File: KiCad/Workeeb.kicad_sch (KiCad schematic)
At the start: 227 parts, among them J1 USB_C_Receptacle_USB2.0, U1 EFM32HG322F64G-C-QFP48

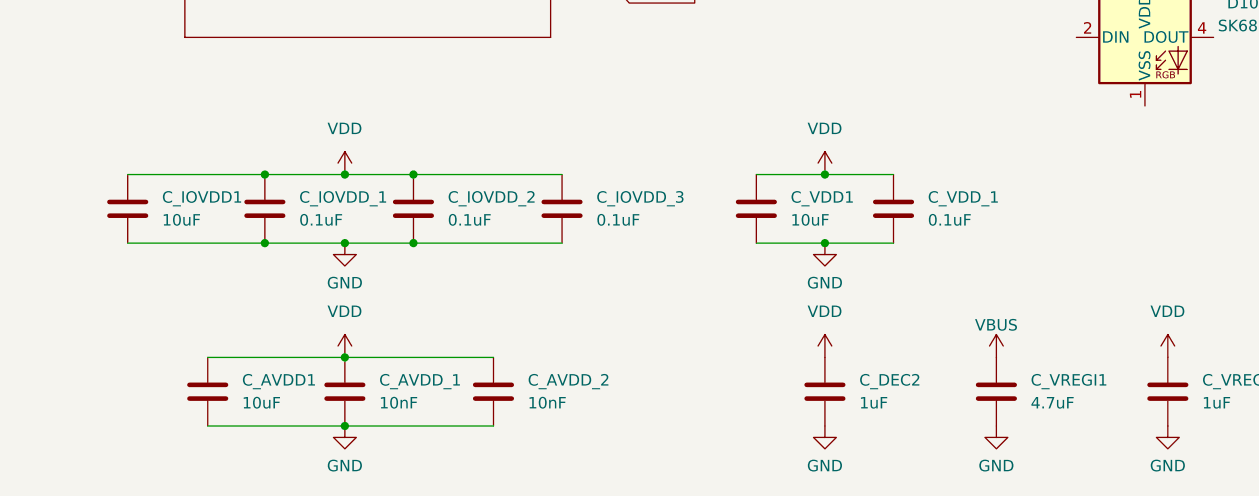
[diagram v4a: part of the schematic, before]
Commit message: Better cap names, start placing decoupling caps
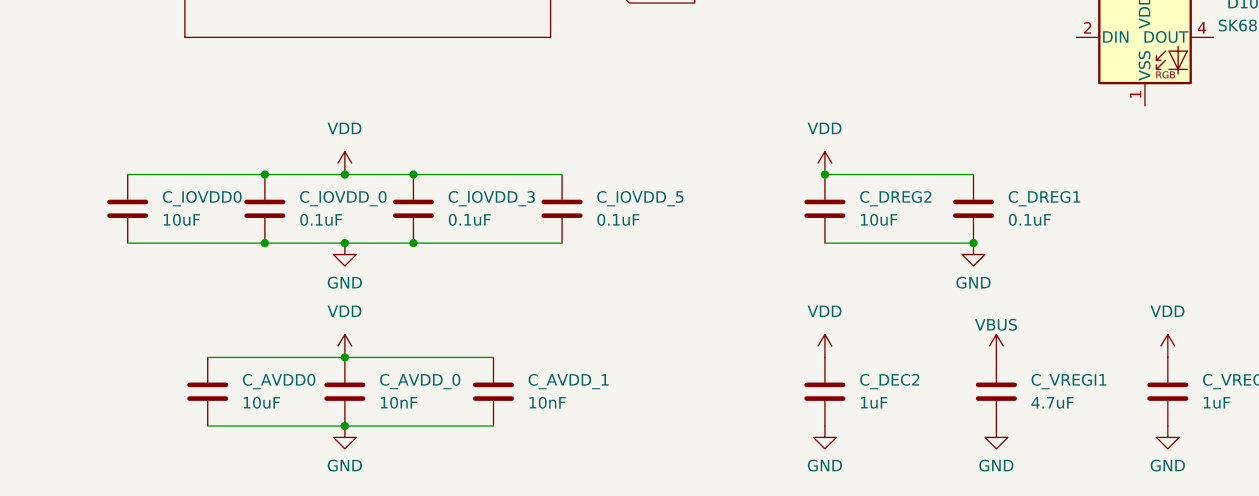
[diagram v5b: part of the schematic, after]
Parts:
- removed C_VDD1: 10uF, Capacitor_SMD:C_0805_2012Metric, symbol Device:C
- removed C_VDD_1: 0.1uF, Capacitor_SMD:C_0805_2012Metric, symbol Device:C
- added C_DREG1: 0.1uF, Capacitor_SMD:C_0402_1005Metric, symbol Device:C
- added C_DREG2: 10uF, Capacitor_SMD:C_0402_1005Metric, symbol Device:C
- C_AVDD0: renamed from C_AVDD1; footprint Capacitor_SMD:C_0805_2012Metric -> Capacitor_SMD:C_0402_1005Metric
- C_AVDD_0: renamed from C_AVDD_1; footprint Capacitor_SMD:C_0805_2012Metric -> Capacitor_SMD:C_0402_1005Metric
- C_AVDD_1: renamed from C_AVDD_2; footprint Capacitor_SMD:C_0805_2012Metric -> Capacitor_SMD:C_0402_1005Metric
- C_DEC1, C_DEC2, C_RESET1, C_VREGI1, C_VREGO1: footprint Capacitor_SMD:C_0805_2012Metric -> Capacitor_SMD:C_0402_1005Metric
- C_IOVDD0: renamed from C_IOVDD1; footprint Capacitor_SMD:C_0805_2012Metric -> Capacitor_SMD:C_0402_1005Metric
- C_IOVDD_0: renamed from C_IOVDD_1; footprint Capacitor_SMD:C_0805_2012Metric -> Capacitor_SMD:C_0402_1005Metric
- C_IOVDD_3: renamed from C_IOVDD_2; footprint Capacitor_SMD:C_0805_2012Metric -> Capacitor_SMD:C_0402_1005Metric
- C_IOVDD_5: renamed from C_IOVDD_3; footprint Capacitor_SMD:C_0805_2012Metric -> Capacitor_SMD:C_0402_1005Metric
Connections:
- net GND: now also C_DREG1.2, C_DREG2.2
- net VDD: now also C_DREG1.1, C_DREG2.1

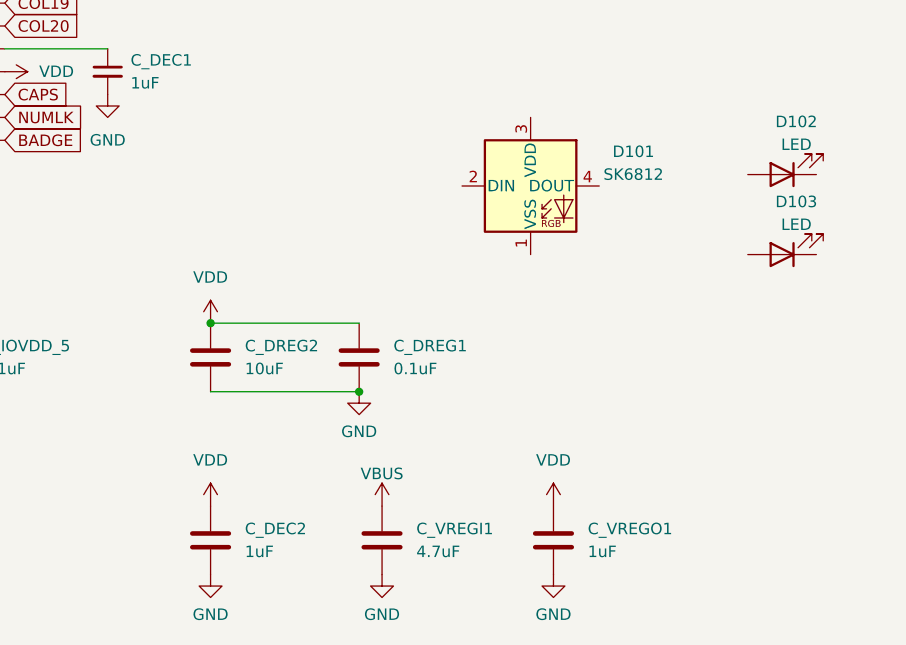
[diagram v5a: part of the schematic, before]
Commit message: Work towards getting decoupling caps and col routes in place
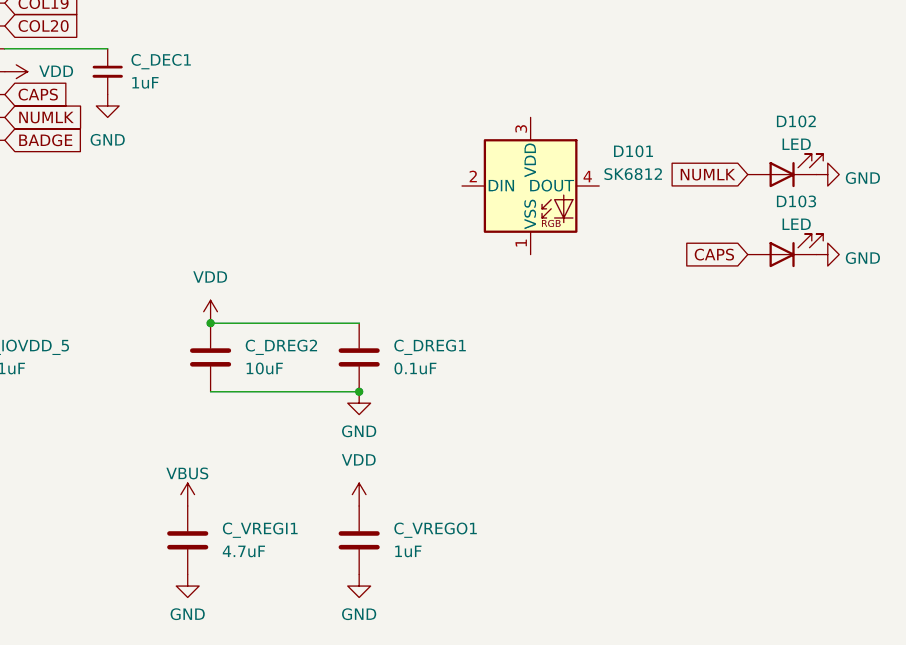
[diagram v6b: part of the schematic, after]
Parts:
- removed C_DEC2: 1uF, Capacitor_SMD:C_0402_1005Metric, symbol Device:C
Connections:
- net CAPS: now also D103.2 (A)
- net GND: now also D102.1 (K), D103.1 (K)
- net NUMLK: now also D102.2 (A)
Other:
- moved on the sheet: C_VREGI1, C_VREGO1

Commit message: Draft finish PCB
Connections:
- net BADGE: now also D101.2 (DIN)
- net GND: now also D101.1 (VSS)
- net VDD: now also D101.3 (VDD)
- no-connect marks 5 -> 6
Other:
- moved on the sheet: D101
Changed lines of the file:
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@@
   (no_connect (at 308.61 100.33))
   (no_connect (at 308.61 107.95))
+  (no_connect (at 421.64 113.03))
   (no_connect (at 330.2 11.43))
   (no_connect (at 330.2 8.89))
@@
     )
   )
+  (global_label "BADGE" (shape input) (at 406.4 113.03 180) (fields_autoplaced)
+    (effects (font (size 1.27 1.27)) (justify right))
+    (property "Intersheet References" "${INTERSHEET_REFS}" (id 0) (at 398.0282 113.1094 0)
+      (effects (font (size 1.27 1.27)) (justify right) hide)
+    )
+  )
   (global_label "COL6" (shape input) (at 81.28 24.13 90) (fields_autoplaced)
     (effects (font (size 1.27 1.27)) (justify left))
@@
     (pin "2")
   )
+  (symbol (lib_id "power:VDD") (at 414.02 105.41 0) (unit 1)
+    (in_bom yes) (on_board yes) (fields_autoplaced)
+    (property "Reference" "#PWR?" (id 0) (at 414.02 109.22 0)
+      (effects (font (size 1.27 1.27)) hide)
+    )
+    (property "Value" "VDD" (id 1) (at 414.02 100.33 0))
+    (property "Footprint" "" (id 2) (at 414.02 105.41 0)
+      (effects (font (size 1.27 1.27)) hide)
+    )
+    (property "Datasheet" "" (id 3) (at 414.02 105.41 0)
+      (effects (font (size 1.27 1.27)) hide)
+    )
+    (pin "1")
+  )
   (symbol (lib_id "power:GND") (at 314.96 19.05 0) (unit 1)
     (in_bom yes) (on_board yes) (fields_autoplaced)
@@
     (pin "2")
   )
+  (symbol (lib_id "power:GND") (at 414.02 120.65 0) (unit 1)
+    (in_bom yes) (on_board yes) (fields_autoplaced)
+    (property "Reference" "#PWR?" (id 0) (at 414.02 127 0)
+      (effects (font (size 1.27 1.27)) hide)
+    )
+    (property "Value" "GND" (id 1) (at 414.02 125.73 0))
+    (property "Footprint" "" (id 2) (at 414.02 120.65 0)
+      (effects (font (size 1.27 1.27)) hide)
+    )
+    (property "Datasheet" "" (id 3) (at 414.02 120.65 0)
+      (effects (font (size 1.27 1.27)) hide)
+    )
+    (pin "1")
+  )
   (symbol (lib_id "Device:D_Small") (at 191.77 106.68 90) (unit 1)
     (in_bom yes) (on_board yes) (fields_autoplaced)
@@
     (pin "1")
   )
-  (symbol (lib_id "LED:SK6812") (at 422.91 113.03 0) (unit 1)
+  (symbol (lib_id "LED:SK6812") (at 414.02 113.03 0) (unit 1)
     (in_bom yes) (on_board yes)
-    (property "Reference" "D101" (id 0) (at 434.34 109.22 0))
-    (property "Value" "SK6812" (id 1) (at 434.34 111.7569 0))
-    (property "Footprint" "LED_SMD:LED_SK6812_PLCC4_5.0x5.0mm_P3.2mm" (id 2) (at 424.18 120.65 0)
+    (property "Reference" "D101" (id 0) (at 425.45 109.22 0))
+    (property "Value" "SK6812" (id 1) (at 425.45 111.7569 0))
+    (property "Footprint" "LED_SMD:LED_SK6812_PLCC4_5.0x5.0mm_P3.2mm" (id 2) (at 415.29 120.65 0)
       (effects (font (size 1.27 1.27)) (justify left top) hide)
     )
-    (property "Datasheet" "https://cdn-shop.adafruit.com/product-files/1138/SK6812+LED+datasheet+.pdf" (id 3) (at 425.45 122.555 0)
+    (property "Datasheet" "https://cdn-shop.adafruit.com/product-files/1138/SK6812+LED+datasheet+.pdf" (id 3) (at 416.56 122.555 0)
       (effects (font (size 1.27 1.27)) (justify left top) hide)
     )
@@
       (reference "#PWR?") (unit 1) (value "GND") (footprint "")
     )
+    (path "/46aac11a-2abe-4559-b491-aff6f4746b6e"
+      (reference "#PWR?") (unit 1) (value "VDD") (footprint "")
+    )
     (path "/8a2f823a-66e8-4eee-b4fd-b8bcef453f75"
       (reference "#PWR?") (unit 1) (value "GND") (footprint "")
     )
+    (path "/9b684ef8-51c6-4b44-b186-a79d2f20a8b1"
+      (reference "#PWR?") (unit 1) (value "GND") (footprint "")
+    )

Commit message: Add resistors for white LEDs
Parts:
- added R_CAPS, R_NUMLK: 10, Resistor_SMD:R_0805_2012Metric, symbol Device:R
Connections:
- net CAPS: now also R_CAPS.1; no longer D103.2 (A)
- net NUMLK: now also R_NUMLK.1; no longer D102.2 (A)
- new net: D103.2 (A), R_CAPS.2
- new net: D102.2 (A), R_NUMLK.2
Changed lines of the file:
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@@
     )
   )
-  (global_label "NUMLK" (shape input) (at 447.04 111.76 180) (fields_autoplaced)
+  (global_label "NUMLK" (shape input) (at 439.42 111.76 180) (fields_autoplaced)
     (effects (font (size 1.27 1.27)) (justify right))
-    (property "Intersheet References" "${INTERSHEET_REFS}" (id 0) (at 438.3053 111.6806 0)
+    (property "Intersheet References" "${INTERSHEET_REFS}" (id 0) (at 430.6853 111.6806 0)
       (effects (font (size 1.27 1.27)) (justify right) hide)
     )
@@
     )
   )
-  (global_label "CAPS" (shape input) (at 447.04 120.65 180) (fields_autoplaced)
+  (global_label "CAPS" (shape input) (at 439.42 120.65 180) (fields_autoplaced)
     (effects (font (size 1.27 1.27)) (justify right))
-    (property "Intersheet References" "${INTERSHEET_REFS}" (id 0) (at 439.8777 120.5706 0)
+    (property "Intersheet References" "${INTERSHEET_REFS}" (id 0) (at 432.2577 120.5706 0)
       (effects (font (size 1.27 1.27)) (justify right) hide)
     )
@@
     (pin "2")
   )
+  (symbol (lib_id "Device:R") (at 443.23 120.65 90) (unit 1)
+    (in_bom yes) (on_board yes)
+    (property "Reference" "R_CAPS" (id 0) (at 443.23 118.11 90))
+    (property "Value" "10" (id 1) (at 443.23 120.65 90))
+    (property "Footprint" "Resistor_SMD:R_0805_2012Metric" (id 2) (at 443.23 122.428 90)
+      (effects (font (size 1.27 1.27)) hide)
+    )
+    (property "Datasheet" "~" (id 3) (at 443.23 120.65 0)
+      (effects (font (size 1.27 1.27)) hide)
+    )
+    (pin "1")
+    (pin "2")
+  )
   (symbol (lib_id "power:GND") (at 454.66 111.76 90) (unit 1)
     (in_bom yes) (on_board yes) (fields_autoplaced)
-    (property "Reference" "#PWR?" (id 0) (at 461.01 111.76 0)
+    (property "Reference" "#PWR0106" (id 0) (at 461.01 111.76 0)
       (effects (font (size 1.27 1.27)) hide)
     )
@@
   (symbol (lib_id "power:VDD") (at 414.02 105.41 0) (unit 1)
     (in_bom yes) (on_board yes) (fields_autoplaced)
-    (property "Reference" "#PWR?" (id 0) (at 414.02 109.22 0)
+    (property "Reference" "#PWR0103" (id 0) (at 414.02 109.22 0)
       (effects (font (size 1.27 1.27)) hide)
     )
@@
   (symbol (lib_id "power:GND") (at 454.66 120.65 90) (unit 1)
     (in_bom yes) (on_board yes) (fields_autoplaced)
-    (property "Reference" "#PWR?" (id 0) (at 461.01 120.65 0)
+    (property "Reference" "#PWR0105" (id 0) (at 461.01 120.65 0)
       (effects (font (size 1.27 1.27)) hide)
     )
@@
   (symbol (lib_id "power:GND") (at 414.02 120.65 0) (unit 1)
     (in_bom yes) (on_board yes) (fields_autoplaced)
-    (property "Reference" "#PWR?" (id 0) (at 414.02 127 0)
+    (property "Reference" "#PWR0104" (id 0) (at 414.02 127 0)
       (effects (font (size 1.27 1.27)) hide)
     )
@@
     (pin "1")
   )
+  (symbol (lib_id "Device:R") (at 443.23 111.76 90) (unit 1)
+    (in_bom yes) (on_board yes)
+    (property "Reference" "R_NUMLK" (id 0) (at 443.23 109.22 90))
+    (property "Value" "10" (id 1) (at 443.23 111.76 90))
+    (property "Footprint" "Resistor_SMD:R_0805_2012Metric" (id 2) (at 443.23 113.538 90)
+      (effects (font (size 1.27 1.27)) hide)
+    )
+    (property "Datasheet" "~" (id 3) (at 443.23 111.76 0)
+      (effects (font (size 1.27 1.27)) hide)
+    )
+    (pin "1")
+    (pin "2")
+  )
   (symbol (lib_id "Device:D_Small") (at 49.53 66.04 90) (unit 1)
     (in_bom yes) (on_board yes) (fields_autoplaced)
@@
       (reference "#PWR0102") (unit 1) (value "GND") (footprint "")
     )
-    (path "/12929197-7764-4821-9b5a-399a8516c1cc"
-      (reference "#PWR?") (unit 1) (value "GND") (footprint "")
-    )
     (path "/46aac11a-2abe-4559-b491-aff6f4746b6e"
-      (reference "#PWR?") (unit 1) (value "VDD") (footprint "")
+      (reference "#PWR0103") (unit 1) (value "VDD") (footprint "")
+    )
+    (path "/9b684ef8-51c6-4b44-b186-a79d2f20a8b1"
+      (reference "#PWR0104") (unit 1) (value "GND") (footprint "")
     )
     (path "/8a2f823a-66e8-4eee-b4fd-b8bcef453f75"
-      (reference "#PWR?") (unit 1) (value "GND") (footprint "")
+      (reference "#PWR0105") (unit 1) (value "GND") (footprint "")
     )
-    (path "/9b684ef8-51c6-4b44-b186-a79d2f20a8b1"
-      (reference "#PWR?") (unit 1) (value "GND") (footprint "")
+    (path "/12929197-7764-4821-9b5a-399a8516c1cc"
+      (reference "#PWR0106") (unit 1) (value "GND") (footprint "")
     )
     (path "/91331fd8-6759-4ae9-a812-851047971552"
@@
       (reference "MX100") (unit 1) (value "numEnter") (footprint "MX_Only:MXOnly-2U-VerticalStabilizers-NoLED")
     )
+    (path "/0fff7ce4-a8e7-44cd-ae3c-b49dae575d0f"
+      (reference "R_CAPS") (unit 1) (value "10") (footprint "Resistor_SMD:R_0805_2012Metric")
+    )
     (path "/95da3e95-4c59-46e8-9744-59a7567d7f21"
       (reference "R_CC1") (unit 1) (value "5.1k") (footprint "Resistor_SMD:R_0805_2012Metric")
@@
       (reference "R_DMPU1") (unit 1) (value "4.7K") (footprint "Resistor_SMD:R_0805_2012Metric")
     )
+    (path "/a840eb2a-84fd-40d8-ab3f-ff2711691f52"
+      (reference "R_NUMLK") (unit 1) (value "10") (footprint "Resistor_SMD:R_0805_2012Metric")
+    )
     (path "/ec0c6572-a860-4bd5-b379-196b962533e8"
